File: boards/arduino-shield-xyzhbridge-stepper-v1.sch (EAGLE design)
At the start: 21 parts, among them IC1 2967-MP6500, IC3 2967-MP6500, J4 ARDUINO_R3_SHIELD, J9 455-1750-1-ND

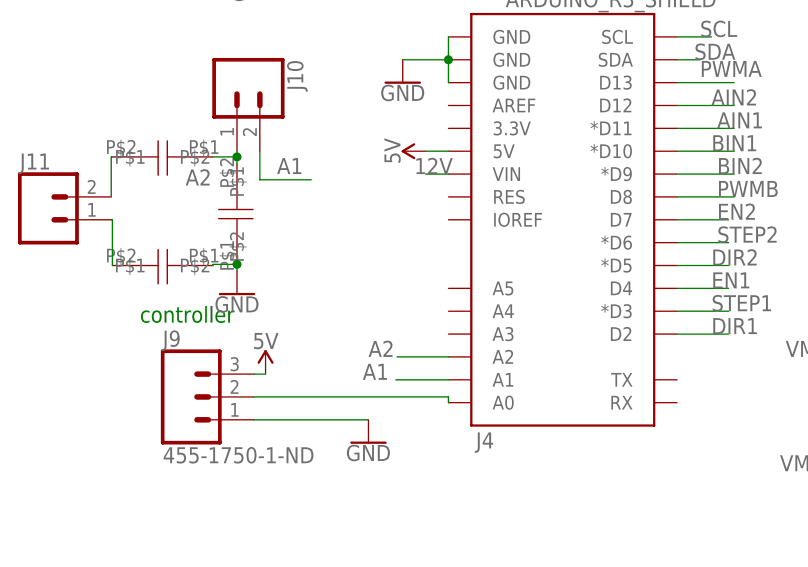
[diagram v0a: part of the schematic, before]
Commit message: finishing touches on a draft of the full control board with slimezistor etc
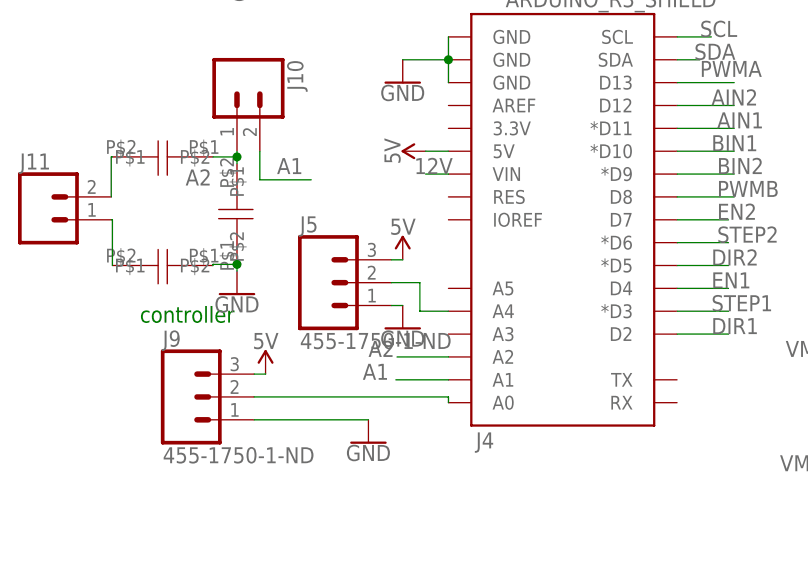
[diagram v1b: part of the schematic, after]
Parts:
- added J5: 455-1750-1-ND, SparkFun-Connectors:CONN_03
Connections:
- new net N$9: J4.A4, J5.2
- net 5V: now also J5.3
- net GND: now also J5.1
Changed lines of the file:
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@@
 <part name="J16" library="SparkFun-Connectors" deviceset="CONN_01" device=""/>
 <part name="J17" library="SparkFun-Connectors" deviceset="CONN_01" device=""/>
+<part name="J5" library="SparkFun-Connectors" deviceset="CONN_03" device="" value="455-1750-1-ND"/>
+<part name="GND7" library="SparkFun-PowerSymbols" deviceset="GND" device=""/>
+<part name="SUPPLY1" library="SparkFun-PowerSymbols" deviceset="5V" device=""/>
 </parts>
 <sheets>
@@
 <attribute name="NAME" x="104.14" y="47.752" size="1.778" layer="95" font="vector" rot="R180"/>
 </instance>
+<instance part="J5" gate="J$1" x="34.29" y="85.725" smashed="yes">
+<attribute name="VALUE" x="31.75" y="78.359" size="1.778" layer="96" font="vector"/>
+<attribute name="NAME" x="31.75" y="91.313" size="1.778" layer="95" font="vector"/>
+</instance>
+<instance part="GND7" gate="1" x="43.18" y="80.645" smashed="yes">
+<attribute name="VALUE" x="43.18" y="80.391" size="1.778" layer="96" align="top-center"/>
+</instance>
+<instance part="SUPPLY1" gate="G$1" x="43.18" y="88.265" smashed="yes">
+<attribute name="VALUE" x="43.18" y="91.059" size="1.778" layer="96" align="bottom-center"/>
+</instance>
 </instances>
 <busses>
@@
 <label x="24.13" y="121.92" size="1.778" layer="95" rot="R270"/>
 </segment>
+<segment>
+<pinref part="J5" gate="J$1" pin="1"/>
+<pinref part="GND7" gate="1" pin="GND"/>
+<wire x1="43.18" y1="83.185" x2="41.91" y2="83.185" width="0.1524" layer="91"/>
+</segment>
 </net>
 <net name="DIR1" class="0">
@@
 <label x="26.67" y="121.92" size="1.778" layer="95"/>
 </segment>
+<segment>
+<pinref part="J5" gate="J$1" pin="3"/>
+<pinref part="SUPPLY1" gate="G$1" pin="5V"/>
+<wire x1="43.18" y1="88.265" x2="41.91" y2="88.265" width="0.1524" layer="91"/>
+</segment>
 </net>
 <net name="PWMB" class="0">
@@
 </segment>
 </net>
+<net name="N$9" class="0">
+<segment>
+<pinref part="J4" gate="G$1" pin="A4"/>
+<wire x1="48.26" y1="82.55" x2="45.085" y2="82.55" width="0.1524" layer="91"/>
+<wire x1="45.085" y1="82.55" x2="45.085" y2="85.725" width="0.1524" layer="91"/>
+<pinref part="J5" gate="J$1" pin="2"/>
+<wire x1="45.085" y1="85.725" x2="41.91" y2="85.725" width="0.1524" layer="91"/>
+</segment>
+</net>

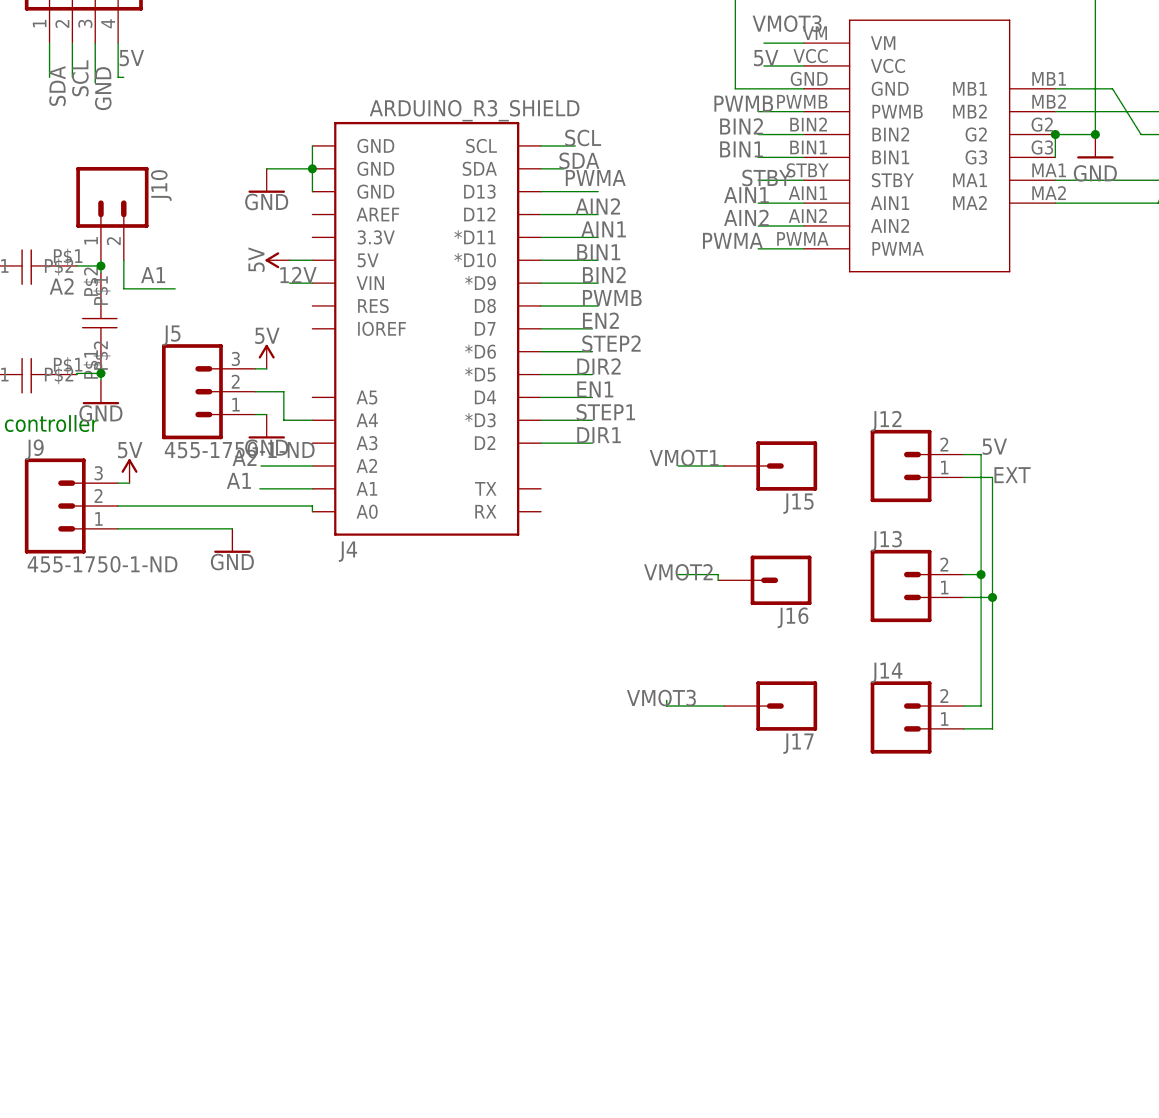
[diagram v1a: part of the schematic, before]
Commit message: two new boards, xyz and slime and xyzhbridge and slime
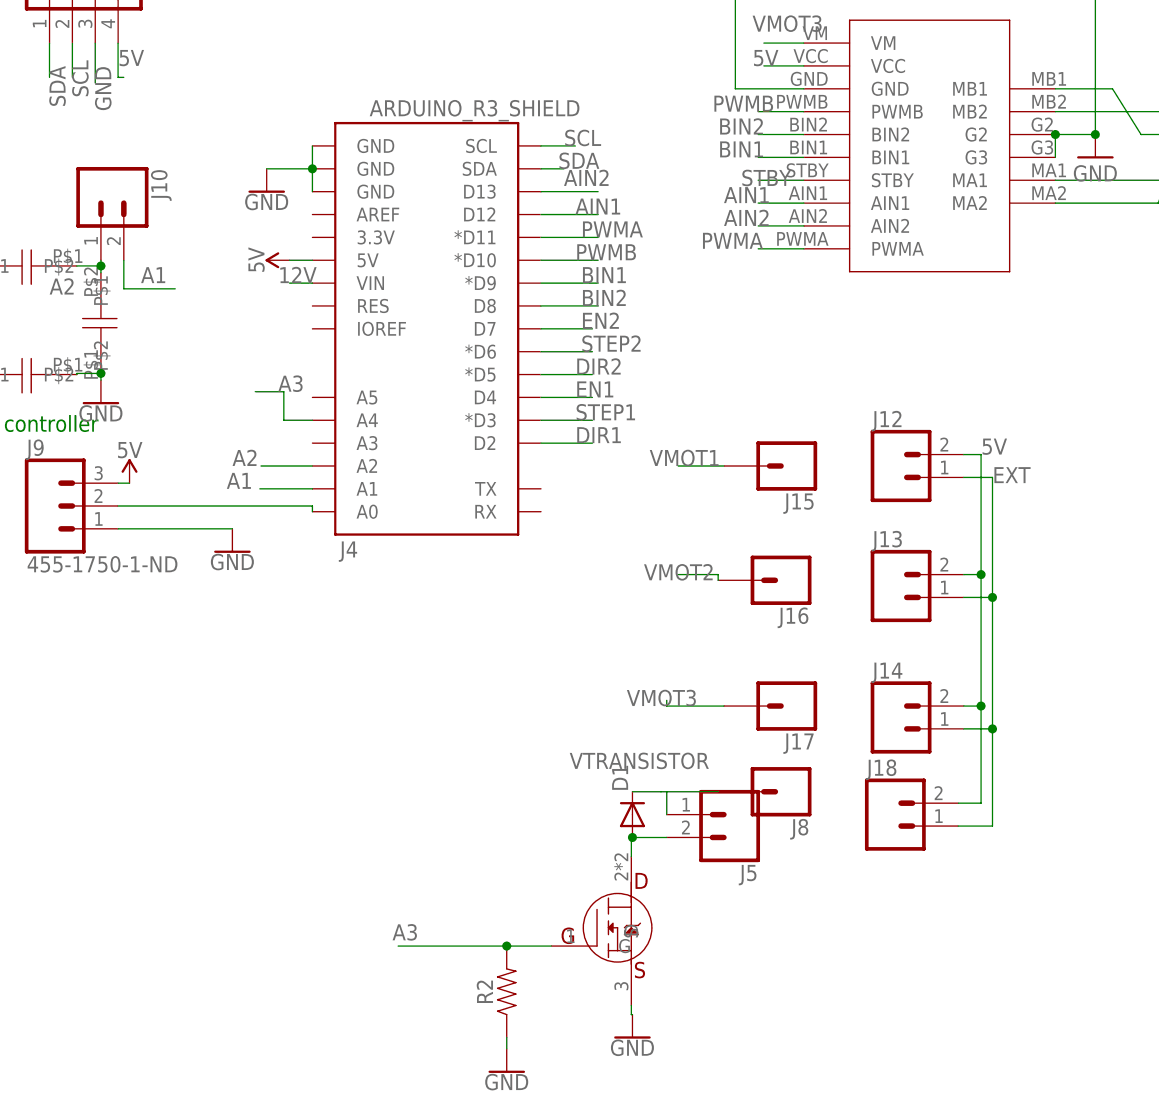
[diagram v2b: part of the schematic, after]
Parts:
- added D1: (no value), diode:DIODE-DO-214AC
- added J18: (no value), SparkFun-Connectors:CONN_02
- added J8: (no value), SparkFun-Connectors:CONN_01
- added R2: (no value), SparkFun-Resistors:RESISTORAXIAL-0.3
- added U$5: IRFL024NPBF, spietz-library-2:IRFL024NPBF
- J5: value 455-1750-1-ND -> (none); device SparkFun-Connectors:CONN_03 -> SparkFun-Connectors:CONN_02
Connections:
- removed net N$9: J4.A4, J5.2
- new net A3: J4.A4, R2.2, U$5.G
- new net N$18: D1.A, J5.2, U$5.D
- new net VTRANSISTOR: D1.C, J5.1, J8.1
- net 5V: now also J18.2; no longer J5.3
- net AIN1: now also J4.D12; no longer J4.*D11
- net AIN2: now also J4.D13; no longer J4.D12
- net BIN1: now also J4.*D9; no longer J4.*D10
- net BIN2: now also J4.D8; no longer J4.*D9
- net EXT: now also J18.1
- net GND: now also R2.1, U$5.S; no longer J5.1
- net PWMA: now also J4.*D11; no longer J4.D13
- net PWMB: now also J4.*D10; no longer J4.D8
